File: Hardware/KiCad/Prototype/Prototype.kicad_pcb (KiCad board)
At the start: 2 copper layers, 101.6 x 63.5 mm, 36 parts, among them J1 Screw_Terminal_01x02, J2 Conn_01x12, J3 Conn_01x12, J4 USB_C_Receptacle_USB2.0, J5 Micro_SD_Card, SW1 SW_SPST, U1 ATSAMD21G18A-A, U2 MCP1703A-3302_SOT23, U3 ADS122C04IPW, Y1 32.768kHz

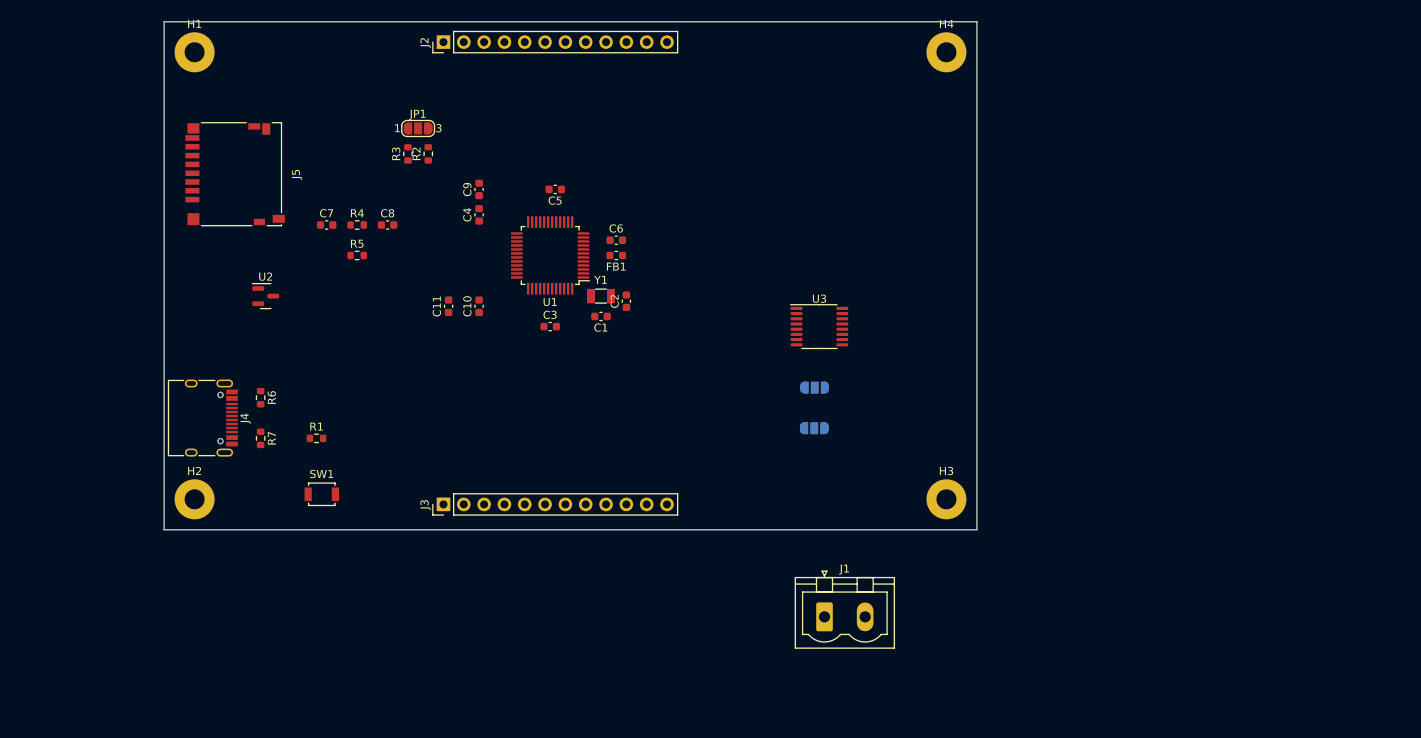
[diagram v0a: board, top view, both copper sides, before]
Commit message: Add v0.3 design
Organize KiCad files by version.
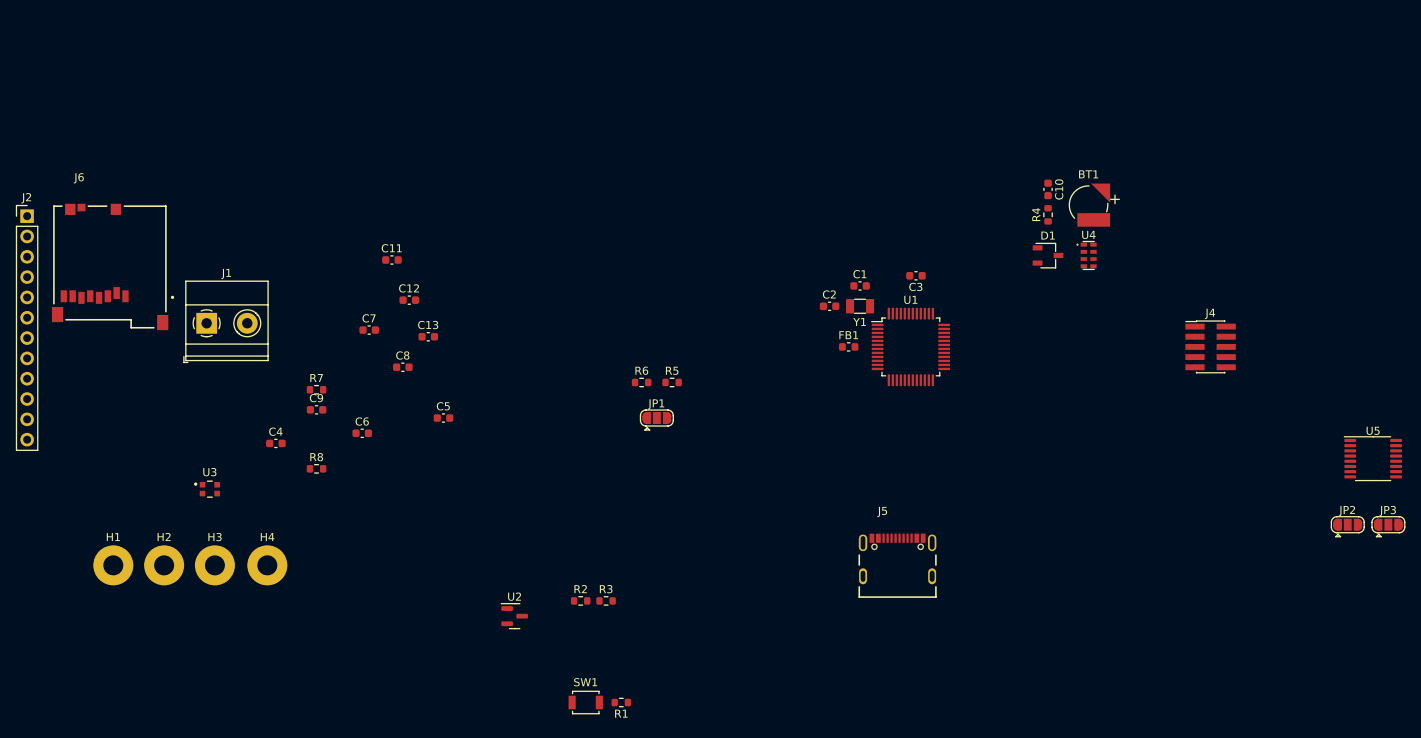
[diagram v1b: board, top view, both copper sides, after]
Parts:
- removed J3: Conn_01x12, Connector_PinHeader_2.54mm:PinHeader_1x12_P2.54mm_Vertical
- added BT1: ML414H, SnapEDA:SEIKO_ML414H_IV01E, F.Cu at (204.5, 91.5)
- added C12: 0.1uF, Capacitor_SMD:C_0603_1608Metric, F.Cu at (119.5, 103.4)
- added C13: 0.1uF, Capacitor_SMD:C_0603_1608Metric, F.Cu at (121.9, 108.0)
- added D1: BAS70-05, Package_TO_SOT_SMD:TSOT-23, F.Cu at (199.4, 97.8)
- added J6: Micro_SD_Card, SnapEDA:GCT_MEM2051-00-195-00-A_REVD1, F.Cu at (82.1, 99.2)
- added R8: 5.1k, Resistor_SMD:R_0603_1608Metric, F.Cu at (108.0, 124.5)
- added U4: RV-8803-C7, SnapEDA:MICROCRYSTAL_RV-8803-C7-TA-QC, F.Cu at (204.5, 97.8)
- added U5: ADS122C04IPW, Package_SO:TSSOP-16_4.4x5mm_P0.65mm, F.Cu at (240.0, 123.2)
- C8: value 0.1uF -> 1uF
- C9: value 1uF -> 0.1uF
- J1: footprint Connector_Phoenix_MSTB:PhoenixContact_MSTBVA_2,5_2-G-5,08_1x02_P5.08mm_Vertical -> TerminalBlock_Phoenix:TerminalBlock_Phoenix_MKDS-1,5-2-5.08_1x02_P5.08mm_Horizontal
- J4: value USB_C_Receptacle_USB2.0 -> Conn_ARM_JTAG_SWD_10; footprint Connector_USB:USB_C_Receptacle_HRO_TYPE-C-31-M-12 -> Connector_PinHeader_1.27mm:PinHeader_2x05_P1.27mm_Vertical_SMD
- J5: value Micro_SD_Card -> USB_C_Receptacle_USB2.0; footprint Connector_Card:microSD_HC_Hirose_DM3D-SF -> SnapEDA:GCT_USB4105-GF-A
- JP1: footprint Jumper:SolderJumper-3_P1.3mm_Open_RoundedPad1.0x1.5mm_NumberLabels -> Jumper:SolderJumper-3_P1.3mm_Open_RoundedPad1.0x1.5mm
- JP2, JP3: moved to F.Cu
- R2: value 2.2k -> 4M
- R3: value 2.2k -> 1M
- R4: value 4M -> 3.3k
- R5: value 1M -> 2.2k
- R6: value 5.1k -> 2.2k
- U3: value ADS122C04IPW -> WS2812_2020; footprint Package_SO:TSSOP-16_4.4x5mm_P0.65mm -> SnapEDA:LED_WS2812-2020
- moved J4 126.7 mm to (219.7, 109.2), turned to 0 degrees
- moved H4 106.4 mm to (101.8, 136.5)
- moved J5 96.9 mm to (180.6, 137.9), turned to 0 degrees
- moved H3 91.8 mm to (95.2, 136.5)
- moved R4 86.4 mm to (199.4, 92.7), turned to 90 degrees
- moved J1 85.5 mm to (94.2, 106.3)
- moved U3 78.9 mm to (94.6, 127.0)
- moved JP3 72.8 mm to (241.9, 131.4), turned to 0 degrees
- moved C10 72.6 mm to (199.4, 89.5), turned to -90 degrees
- moved JP2 68.8 mm to (236.9, 131.4), turned to 0 degrees
- moved H1 64.9 mm to (82.5, 136.5)
- moved R3 61.1 mm to (144.1, 141.0), turned to 0 degrees
- moved R2 59.0 mm to (141.0, 141.0), turned to 0 degrees
- moved J2 56.4 mm to (71.8, 92.9), turned to 0 degrees
- moved U2 50.7 mm to (132.7, 142.9)
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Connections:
- C11 pad 2: Net-(C11-Pad2) -> +3V3
- C8 pad 2: D9/A7 -> +3V3
- C9 pad 2: +3V3 -> D9/A7
- JP2 pad 1: +3V3 -> GND
- JP2 pad 3: GND -> +3V3
- JP3 pad 1: +3V3 -> GND
- JP3 pad 3: GND -> +3V3
- R2 pad 1: SCL -> D9/A7
- R2 pad 2: Net-(JP1-Pad3) -> +BATT
- R3 pad 1: SDA -> GND
- R3 pad 2: Net-(JP1-Pad1) -> D9/A7
- R4 pad 1: D9/A7 -> Net-(BT1-Pad1)
- R4 pad 2: +BATT -> Net-(C10-Pad2)
- R5 pad 1: GND -> SCL
- R5 pad 2: D9/A7 -> Net-(JP1-Pad3)
- R6 pad 1: Net-(J4-PadA5) -> SDA
- R6 pad 2: GND -> Net-(JP1-Pad1)
- R7 pad 1: Net-(J4-PadB5) -> Net-(J5-PadA5)
- U3 pad 1: ADDR_A0 -> unconnected-(U3-Pad1)
- U3 pad 2: ADDR_A1 -> GND
- U3 pad 3: ~{RESET} -> D10
- U3 pad 4: GND -> +3V3
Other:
- board outline removed
